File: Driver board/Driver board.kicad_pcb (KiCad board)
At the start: 2 copper layers, 66 x 100 mm, 46 parts, among them J1 Conn_02x02_Odd_Even, J10 Conn_01x03_Male, J2 Conn_02x02_Odd_Even, J3 Conn_01x02_Male, J4 Conn_01x03_Male, J5 Conn_01x02_Male, J6 Conn_01x03_Male, J7 Conn_02x02_Odd_Even, J8 Conn_02x02_Odd_Even, J9 Conn_01x03_Male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

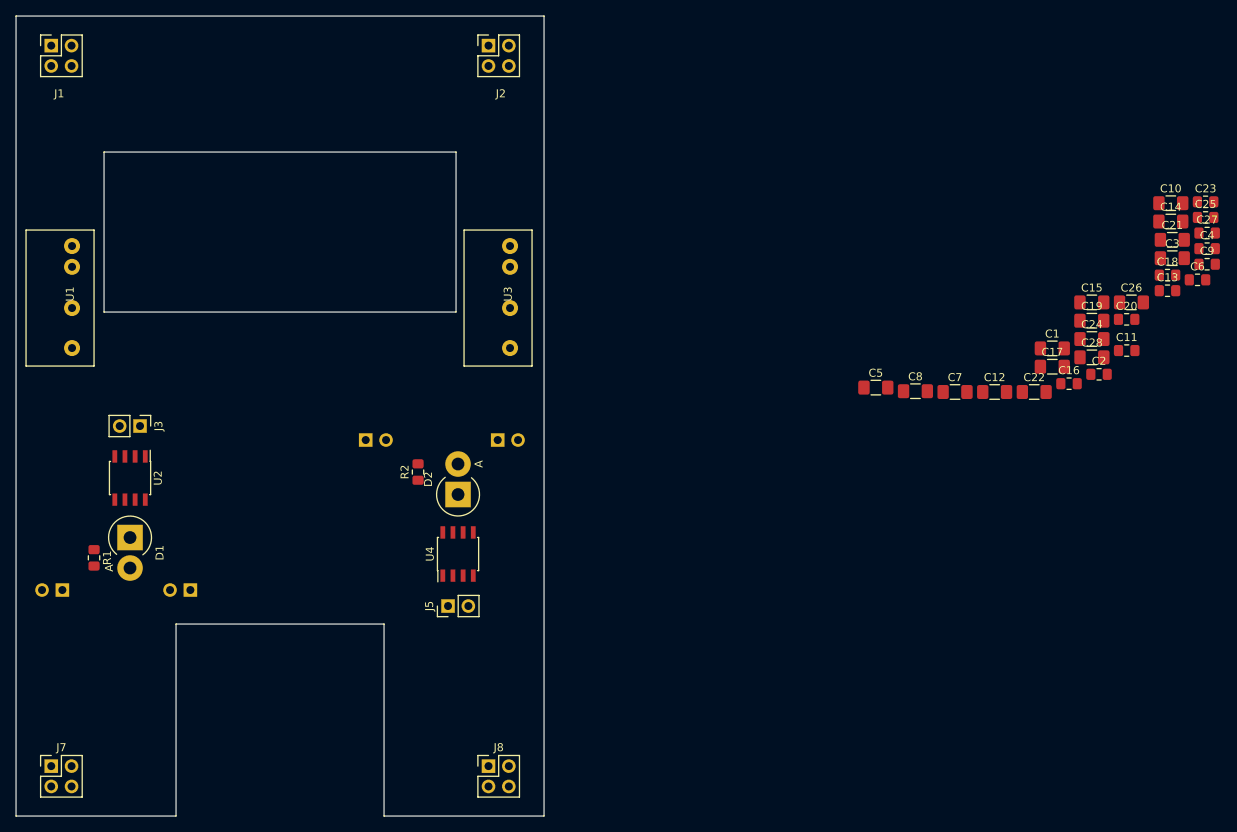
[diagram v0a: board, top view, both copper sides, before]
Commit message: Driver board wired, no decals yet
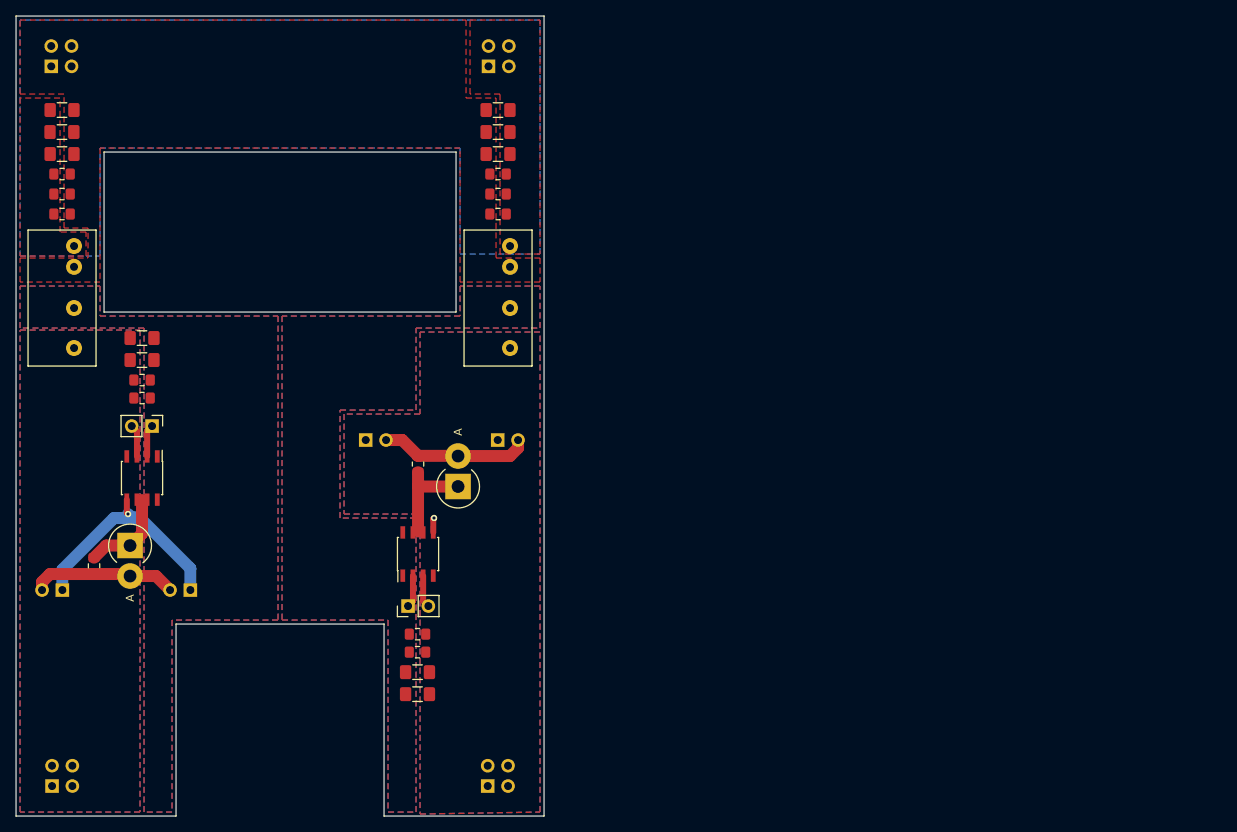
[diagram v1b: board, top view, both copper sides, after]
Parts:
- removed C14, C21, C28, C7: 1u, Capacitor_SMD:C_1206_3216Metric_Pad1.42x1.75mm_HandSolder
- removed C19, C5: 10n, Capacitor_SMD:C_1206_3216Metric_Pad1.42x1.75mm_HandSolder
- removed C20, C6: 100n, Capacitor_SMD:C_0805_2012Metric_Pad1.15x1.40mm_HandSolder
- J1, J2, J7, J8: moved to B.Cu
- moved C9 143.6 mm to (5.75, 19.8)
- moved C10 138.7 mm to (5.75, 17.2)
- moved C13 138.5 mm to (5.75, 24.8)
- moved C11 134.5 mm to (5.75, 22.2)
- moved C4 134.4 mm to (15.8, 47.8)
- moved C3 129.4 mm to (15.8, 43.0)
- moved C12 121.8 mm to (5.75, 11.8)
- moved C2 119.6 mm to (15.8, 45.5)
- moved C1 113.8 mm to (15.8, 40.2)
- moved C8 111.5 mm to (5.74, 14.5)
- moved C18 103.9 mm to (50.2, 77.3), turned to 180 degrees
- moved C15 97.5 mm to (50.2, 84.8), turned to 180 degrees
- moved C27 88.7 mm to (60.2, 24.8), turned to 180 degrees
- moved C23 88.5 mm to (60.2, 19.8), turned to 180 degrees
- moved C25 88.5 mm to (60.2, 22.2), turned to 180 degrees
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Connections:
- C1 pad 1: -BATT -> /VH-_isol
- C15 pad 1: -BATT -> /VL-_isol
- C16 pad 1: -BATT -> /VL-_isol
- C17 pad 1: -BATT -> /VL-_isol
- C18 pad 1: -BATT -> /VL-_isol
- C2 pad 1: -BATT -> /VH-_isol
- C3 pad 1: -BATT -> /VH-_isol
- C4 pad 1: -BATT -> /VH-_isol
- J4 pad 1: -BATT -> /VH-_isol
- J9 pad 1: -BATT -> /VH-_isol
- U1 pad 4: -BATT -> /VH-_isol
- U2 pad 5: -BATT -> /VH-_isol
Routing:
- net /VH-_isol: track 0.00 -> 29.9 mm, vias 0 -> 1
- net Net-(D2-Pad2): track 0.00 -> 18.7 mm
- net Net-(D1-Pad2): track 0.00 -> 18.2 mm
- net Net-(D2-Pad1): track 0.00 -> 13.6 mm
- net Net-(D1-Pad1): track 0.00 -> 12.7 mm
- net Net-(J5-Pad2): track 0.00 -> 4.07 mm
- net Net-(J3-Pad2): track 0.00 -> 4.07 mm
- net Net-(J5-Pad1): track 0.00 -> 4.05 mm
- net Net-(J3-Pad1): track 0.00 -> 4.05 mm
- net /VL-_isol: track 0.00 -> 1.84 mm, vias 0 -> 1
- added copper zone on F.Cu, net +BATT
- added copper zone on B.Cu, net -BATT
- added copper zone on F.Cu, net -BATT
- added copper zone on B.Cu, net /VH+_isol
- added copper zone on F.Cu, net /VH+_isol
- added copper zone on B.Cu, net /VH-_isol
- added copper zone on F.Cu, net /VH-_isol
- added copper zone on B.Cu, net /VL+_isol
- added copper zone on F.Cu, net /VL+_isol
- added copper zone on B.Cu, net /VL-_isol
- added copper zone on F.Cu, net /VL-_isol
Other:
- net class Default: trace_width 2 -> 0.75
